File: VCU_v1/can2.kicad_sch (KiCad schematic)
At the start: 4 parts, among them U12 MCP2562 E/SN

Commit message: p dih r
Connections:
- net CAN2_L: no longer JP3.1 (A)
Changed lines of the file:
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@@
-	)
-	(junction
-		(at 226.06 97.79)
-		(diameter 0)
-		(color 0 0 0 0)
 	)
 	(junction
@@
 	(wire
 		(pts
-			(xy 226.06 73.66) (xy 226.06 97.79)
-		)
-		(stroke
-			(width 0)
-			(type default)
-		)
-	)
-	(wire
-		(pts
 			(xy 186.69 97.79) (xy 203.2 97.79)
 		)
@@
 	(wire
 		(pts
-			(xy 203.2 97.79) (xy 226.06 97.79)
-		)
-		(stroke
-			(width 0)
-			(type default)
-		)
-	)
-	(wire
-		(pts
 			(xy 113.03 71.12) (xy 113.03 78.74)
 		)
@@
 	(wire
 		(pts
-			(xy 203.2 73.66) (xy 226.06 73.66)
-		)
-		(stroke
-			(width 0)
-			(type default)
-		)
-	)
-	(wire
-		(pts
 			(xy 116.84 93.98) (xy 123.19 93.98)
 		)
@@
 	(wire
 		(pts
-			(xy 190.5 78.74) (xy 190.5 82.55)
+			(xy 190.5 69.85) (xy 190.5 82.55)
 		)
 		(stroke
@@
 	(wire
 		(pts
-			(xy 226.06 97.79) (xy 227.33 97.79)
-		)
-		(stroke
-			(width 0)
-			(type default)
-		)
-	)
-	(wire
-		(pts
-			(xy 203.2 76.2) (xy 203.2 73.66)
+			(xy 203.2 97.79) (xy 227.33 97.79)
 		)
 		(stroke
@@
 	(hierarchical_label "CAN2_H"
 		(shape input)
-		(at 190.5 78.74 90)
-		(effects
-			(font
+		(at 190.5 69.85 0)
+		(effects
+			(font

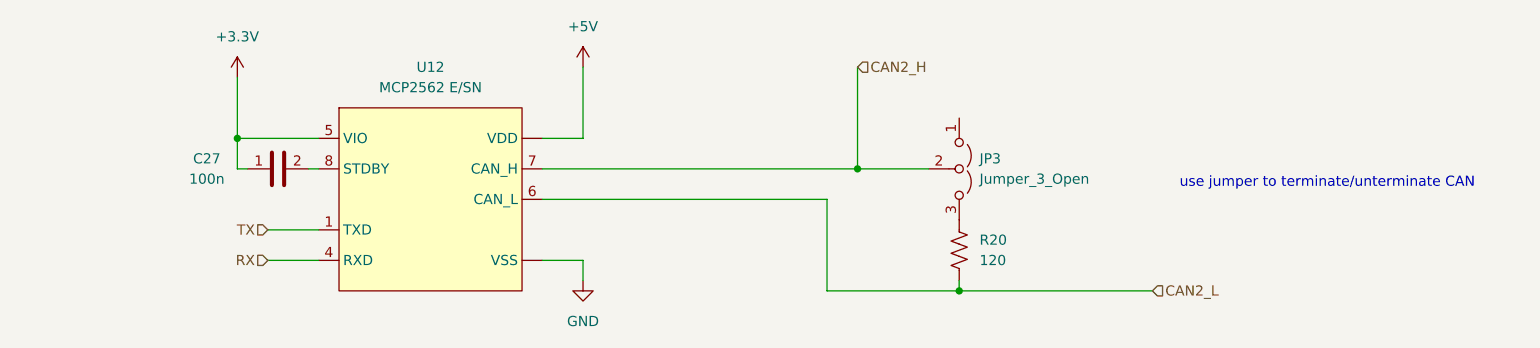
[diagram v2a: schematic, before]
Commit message: v1 schematic (actually) complete, let the layout commence
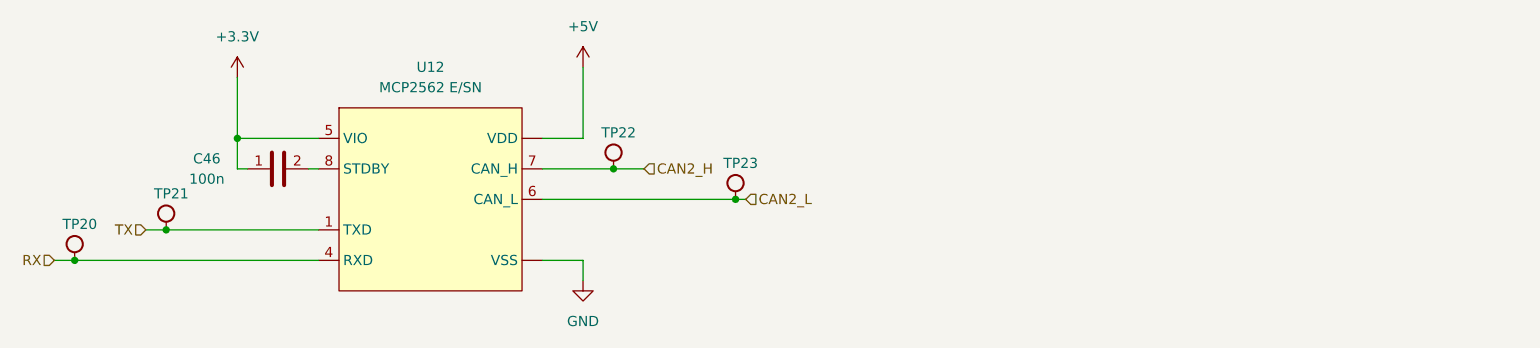
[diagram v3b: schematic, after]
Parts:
- removed JP3: Jumper_3_Open, symbol Jumper:Jumper_3_Open
- removed R20: 120, Resistor_SMD:R_0603_1608Metric_Pad0.98x0.95mm_HandSolder, symbol BFR Resistors:RMCF0603FT120R
- added TP20, TP21, TP22, TP23: RH-5015, TestPoint:TestPoint_Keystone_5015_Micro_Mini, symbol .Test-Point:RH-5015
- U12: footprint (none) -> Package_SO:SOIC-8_3.9x4.9mm_P1.27mm
- renumbered C27 to C46
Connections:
- net CAN2_H: now also TP22.1
- net CAN2_L: now also TP23.1
- net RX: now also TP20.1
- net TX: now also TP21.1
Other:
- note removed: "use jumper to terminate/unterminate CAN"

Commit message: begin pcb design
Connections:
- net +5V: now also U12.3 (VDD); no longer U12. (VSS)
- net GND: now also U12.2 (VSS); no longer U12. (VSS)
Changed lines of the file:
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@@
 		(pin "4"
 		)
-		(pin ""
+		(pin "2"
 		)
 		(pin "7"
@@
 		(pin "6"
 		)
-		(pin ""
+		(pin "3"
 		)
 		(instances

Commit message: vcu placements complete
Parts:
- U12: value MCP2562 E/SN -> MCP2562FD-E/SN; LCSC P/N C53609 -> C124016; Mouser P/N 579-MCP2562-E/SN -> 579-MCP2562FD-E/SN
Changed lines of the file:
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@@
 			)
 		)
-		(property "Value" "MCP2562 E/SN"
+		(property "Value" "MCP2562FD-E/SN"
 			(at 137.16 72.39 0)
 			(effects
@@
 			)
 		)
-		(property "Datasheet" "https://www.mouser.com/datasheet/2/268/20005167C-3443186.pdf"
+		(property "Datasheet" "https://ww1.microchip.com/downloads/en/DeviceDoc/20005284A.pdf"
 			(at 137.16 71.12 0)
 			(effects
@@
 			)
 		)
-		(property "Mouser P/N" "579-MCP2562-E/SN "
+		(property "Mouser P/N" "579-MCP2562FD-E/SN "
 			(at 137.16 71.12 0)
 			(effects
@@
 			)
 		)
-		(property "LCSC P/N" "C53609"
+		(property "LCSC P/N" " C124016"
 			(at 137.16 71.12 0)
 			(effects

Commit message: almost done i promise
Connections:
- net GND: now also C46.2, U12.8 (STDBY)
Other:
- moved on the sheet: C46, TP20, TP21
